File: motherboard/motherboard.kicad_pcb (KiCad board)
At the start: 4 copper layers, 132.9 x 92 mm, 265 parts, among them CN1 PJ-332A-6A (3.5mm Jack), IC1 PI6C557-05BLE, J1 USB_C_Receptacle, J10 DEBUG UART, J11 SYSTEM, J12 5V FAN, J13 Bus_M.2_Socket_E, J14 Micro_SD_Card_Det1, J15 Bus_M.2_Socket_M, J16 USB, J17 USB, J18 USB, J19 USB, J2 20455-040E-76 OLED IPEX, J20 CM3588 Hirose Connector, J22 BATTERY IN, J3 RIGHT SPEAKERS, J4 LEFT SPEAKERS, J5 Outer USB-C, J6 OLED EL POWER, J7 HALL SWITCH, J8 HDMI_A, Q1 2SK3018W, Q10 2SK3018W, Q11 AO3415A, Q12 2SK3018W, Q2 2SK3018W, Q3 L2N7002WT1G, Q4 2SK3018W, Q5 2SK3018W, Q6 WNM6002-3/TR, Q7 WNM6002-3/TR, Q8 WNM6002-3/TR, Q9 WNM6002-3/TR, SW1 PWR, SW2 RESET, SW3 MASK, SW4 RECOVERY, U1 TPD4E02B04, U10 TPD4E02B04, U11 TPD4E02B04, U12 TPD4E02B04, U13 TPD4E02B04, U14 AP2331, U15 TVS2200DRV, U16 TPA2016D2RTJR, U17 TPS564257DRLR, U18 TPD4E02B04, U19 TPD4E02B04, U2 TPD4E02B04, U20 TPS564257DRLR, U21 AP2127K-3.3, U22 CH334F, U23 TPS564257DRLR, U26 AMS1117-1.8, U28 SPI Flash, U29 TVS2200DRV, U3 TPD4E02B04, U4 FUSB302BMPX, U5 SY6280AAC, U6 SY6280AAC, U7 FUSB302BMPX, U8 TPD4E02B04, U9 TPD4E02B04, Y1 25MHz, Y2 12MHz

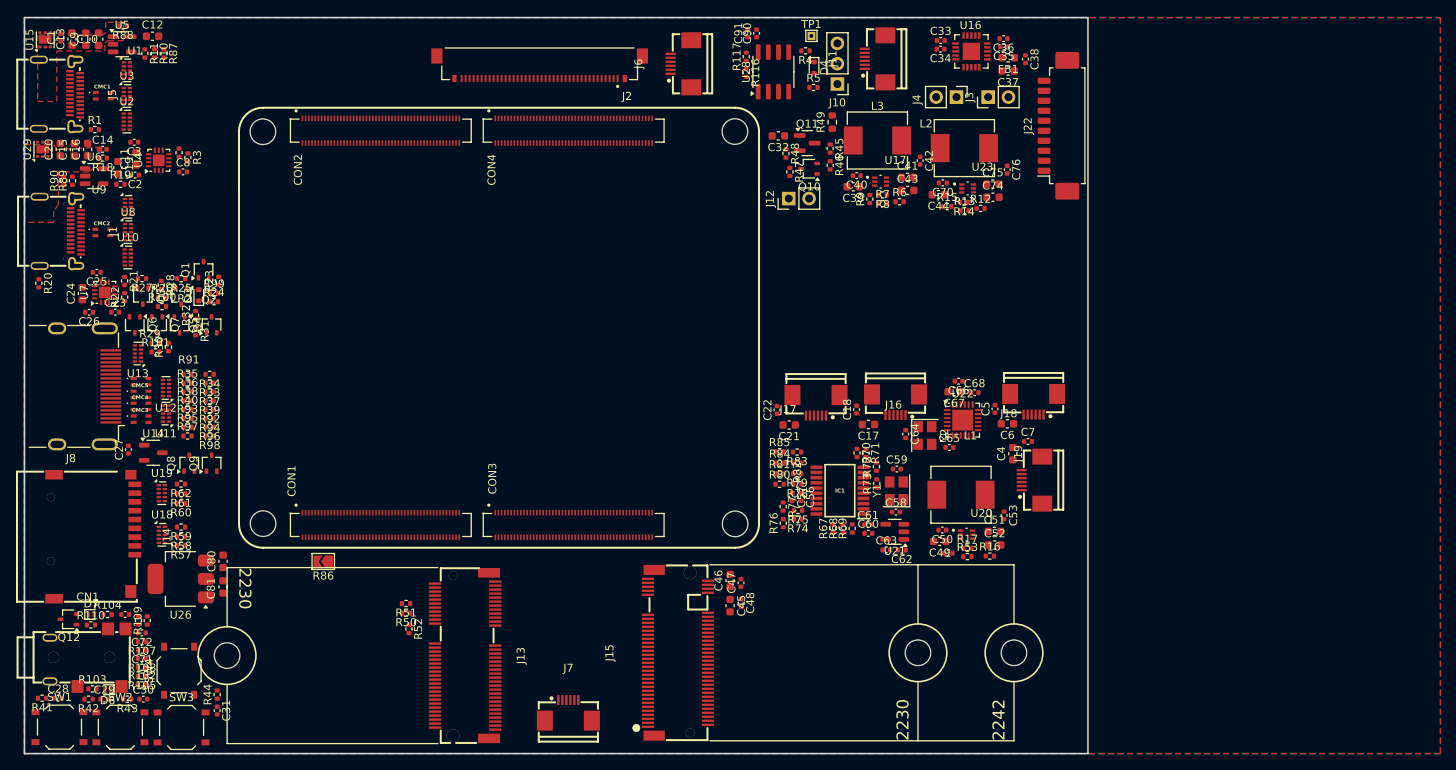
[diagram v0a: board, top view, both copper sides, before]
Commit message: 6 layer for better high speed signaling integrity
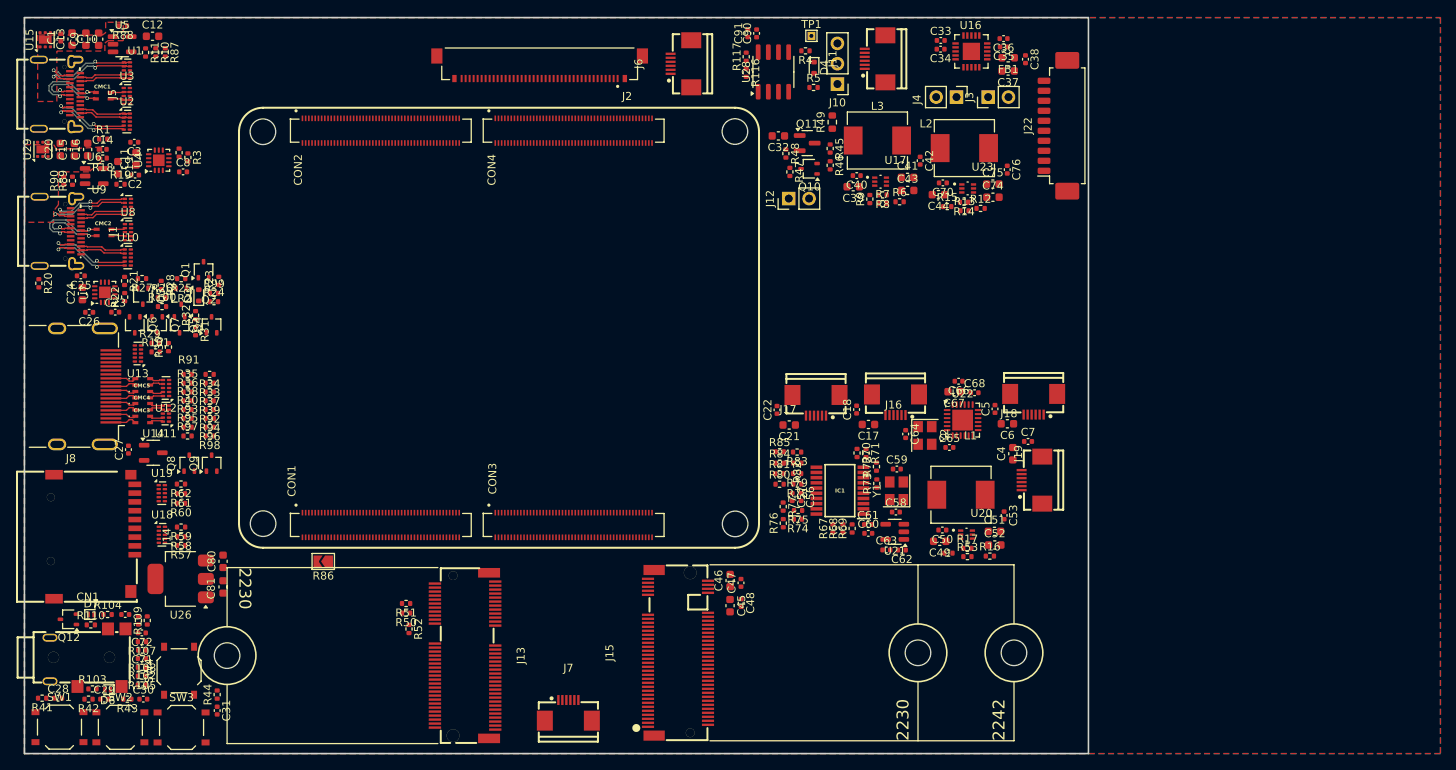
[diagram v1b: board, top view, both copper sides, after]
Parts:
- R54: renamed from 10k; value Resistor_SMD:R_0402_1005Metric -> 10k
- moved C25 2.04 mm to (63.4, 83.7)
- moved R1 1.58 mm to (66.2, 66.6)
- moved CMC3 0.21 mm to (71.1, 101.7)
- moved CMC4 0.21 mm to (71.1, 100.0)
- moved CMC5 0.21 mm to (71.1, 98.5)
- moved CMC6 0.21 mm to (71.1, 97.0)
- moved R10 0.21 mm to (72.8, 55.8)
- moved R87 0.21 mm to (74.0, 55.8)
- moved CMC2 0.16 mm to (66.3, 78.3)
- moved R11 0.15 mm to (71.5, 55.8)
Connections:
- net Net-(CMC2-Pad1) renamed /USBC1/IN_D+
- net Net-(CMC2-Pad2) renamed /USBC1/IN_D-
- CMC3 pad 1: unconnected-(CMC3-Pad1) -> /HDMI_TX/IN_TX2N
- CMC3 pad 2: unconnected-(CMC3-Pad2) -> /HDMI_TX/IN_TX2P
- CMC4 pad 1: unconnected-(CMC4-Pad1) -> /HDMI_TX/IN_TX1N
- CMC4 pad 2: unconnected-(CMC4-Pad2) -> /HDMI_TX/IN_TX1P
- CMC5 pad 1: unconnected-(CMC5-Pad1) -> /HDMI_TX/IN_TX0N
- CMC5 pad 2: unconnected-(CMC5-Pad2) -> /HDMI_TX/IN_TX0P
- CMC6 pad 1: unconnected-(CMC6-Pad1) -> /HDMI_TX/IN_TX3N
- CMC6 pad 2: unconnected-(CMC6-Pad2) -> /HDMI_TX/IN_TX3P
- J8 pad 1: unconnected-(CMC3-Pad2) -> /HDMI_TX/IN_TX2P
- J8 pad 10: unconnected-(CMC6-Pad2) -> /HDMI_TX/IN_TX3P
- J8 pad 12: unconnected-(CMC6-Pad1) -> /HDMI_TX/IN_TX3N
- J8 pad 3: unconnected-(CMC3-Pad1) -> /HDMI_TX/IN_TX2N
- J8 pad 4: unconnected-(CMC4-Pad2) -> /HDMI_TX/IN_TX1P
- J8 pad 6: unconnected-(CMC4-Pad1) -> /HDMI_TX/IN_TX1N
- J8 pad 7: unconnected-(CMC5-Pad2) -> /HDMI_TX/IN_TX0P
- J8 pad 9: unconnected-(CMC5-Pad1) -> /HDMI_TX/IN_TX0N
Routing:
- net /USBC0/RX1+: track 0.00 -> 13.1 mm, vias 0 -> 2
- net /USBC0/RX1-: track 0.00 -> 12.9 mm, vias 0 -> 2
- net /USBC0/IN_D+: track 0.00 -> 11.7 mm, vias 0 -> 2
- net /USBC1/RX1-: track 0.00 -> 11.5 mm, vias 0 -> 2
- net /USBC1/IN_D+: track 0.00 -> 11.4 mm, vias 0 -> 2
- net /USBC1/TX2-: track 0.00 -> 11.2 mm, vias 0 -> 2
- net /USBC1/TX2+: track 0.00 -> 11.1 mm, vias 0 -> 2
- net /USBC1/RX1+: track 0.00 -> 10.7 mm, vias 0 -> 2
- net /USBC0/TX2-: track 0.00 -> 10.3 mm, vias 0 -> 2
- net /USBC0/IN_D-: track 0.00 -> 10.3 mm, vias 0 -> 2
- net /USBC0/TX2+: track 0.00 -> 10.3 mm, vias 0 -> 2
- net /USBC1/IN_D-: track 0.00 -> 10.2 mm, vias 0 -> 2
- net /USBC0/RX2-: track 0.00 -> 6.54 mm
- net /USBC0/RX2+: track 0.00 -> 6.54 mm
- net /USBC0/TX1+: track 0.00 -> 6.48 mm
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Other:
- board size 132.9 x 92 mm -> 133 x 92 mm
- copper layers 4 -> 6

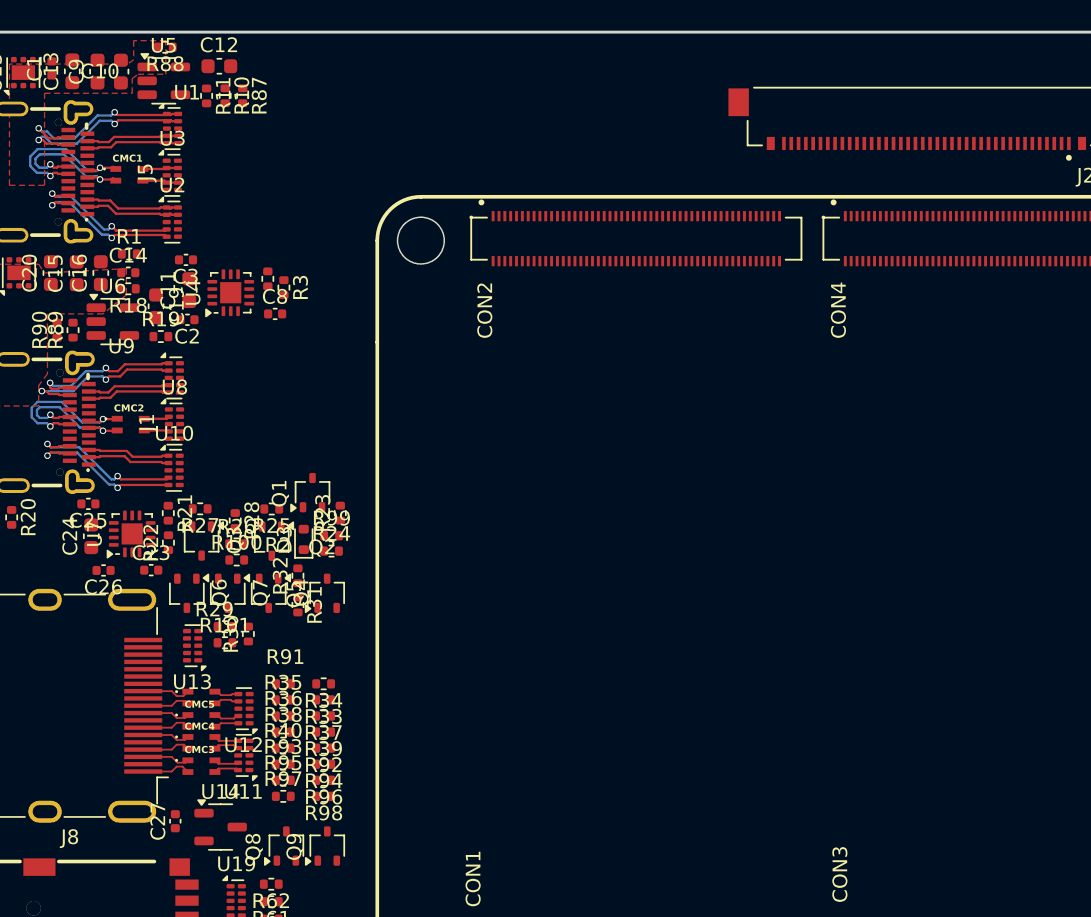
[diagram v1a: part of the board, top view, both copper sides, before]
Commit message: rerouting high speed traces
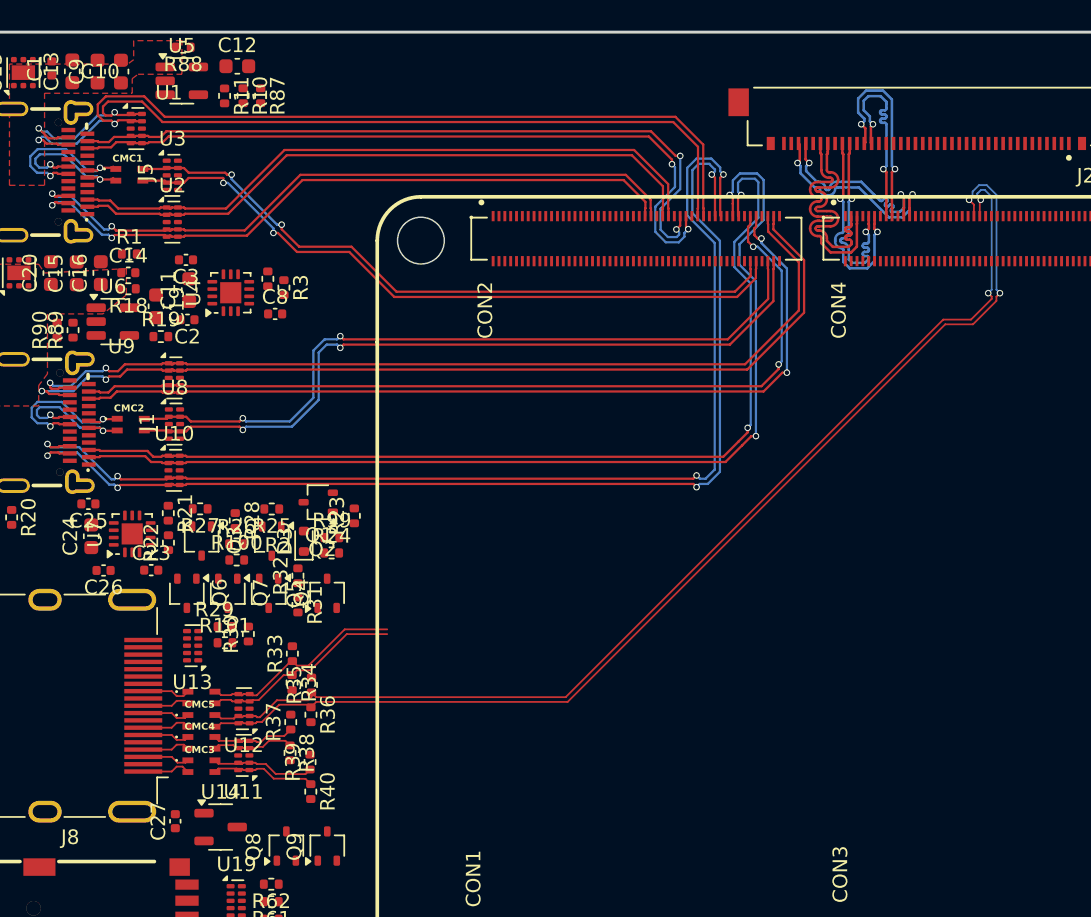
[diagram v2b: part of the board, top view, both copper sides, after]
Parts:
- removed R91, R92, R94, R96, R98: 510, Resistor_SMD:R_0402_1005Metric
- removed R93, R95, R97: 24k, Resistor_SMD:R_0402_1005Metric
- Q2: value 2SK3018W -> Q2
- R33, R34, R36, R38, R40: value 24k -> 499R
- R35, R37, R39: value 510 -> 499R
- U1: value TPD4E02B04 -> U1
- moved R33 3.82 mm to (77.4, 94.0), turned to 90 degrees
- moved R40 3.52 mm to (78.6, 103.4), turned to -90 degrees
- moved U1 2.48 mm to (66.7, 58.0)
- moved R37 2.29 mm to (77.2, 98.6), turned to 90 degrees
- moved R39 2.26 mm to (78.6, 101.4), turned to 90 degrees
- moved R35 2.19 mm to (78.7, 96.1), turned to 90 degrees
- moved R34 2.16 mm to (77.3, 95.9), turned to -90 degrees
- moved R36 1.89 mm to (78.6, 98.1), turned to -90 degrees
- moved R38 1.50 mm to (77.2, 100.7), turned to -90 degrees
- moved C12 1.23 mm to (73.6, 53.8)
- moved R11 1.23 mm to (72.7, 55.8)
- moved R87 1.23 mm to (75.2, 55.8)
- moved R88 1.23 mm to (69.9, 52.5)
- moved U5 1.23 mm to (69.8, 54.8)
- moved R10 1.23 mm to (74.0, 55.8)
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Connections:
- R33 pad 1: /HDMI_TX/HDMI0_TX3P -> /HDMI_TX/HDMI0_TX3N
- R34 pad 1: /HDMI_TX/HDMI0_TX3N -> /HDMI_TX/HDMI0_TX3P
- R35 pad 1: /HDMI_TX/HDMI0_TX3P -> /HDMI_TX/HDMI0_TX0N
- R35 pad 2: Net-(Q6-D) -> Net-(Q7-D)
- R36 pad 1: /HDMI_TX/HDMI0_TX0N -> /HDMI_TX/HDMI0_TX0P
- R37 pad 1: /HDMI_TX/HDMI0_TX0N -> /HDMI_TX/HDMI0_TX1N
- R37 pad 2: Net-(Q7-D) -> Net-(Q8-D)
- R38 pad 1: /HDMI_TX/HDMI0_TX0P -> /HDMI_TX/HDMI0_TX1P
- R38 pad 2: Net-(Q7-D) -> Net-(Q8-D)
- R39 pad 1: /HDMI_TX/HDMI0_TX0P -> /HDMI_TX/HDMI0_TX2N
- R39 pad 2: Net-(Q7-D) -> Net-(Q9-D)
- R40 pad 1: /HDMI_TX/HDMI0_TX1N -> /HDMI_TX/HDMI0_TX2P
- R40 pad 2: Net-(Q8-D) -> Net-(Q9-D)
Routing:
- net /HDMI_TX/HDMI0_TX0P: track 1.70 -> 77.2 mm, vias 0 -> 2
- net /HDMI_TX/HDMI0_TX0N: track 1.78 -> 75.9 mm, vias 0 -> 2
- net /USBC1/TX2-: track 11.2 -> 76.8 mm, vias 2 -> 4
- net /USBC1/TX2+: track 11.1 -> 76.1 mm, vias 2 -> 4
- net /USBC1/RX2+: track 5.67 -> 70.5 mm, vias 0 -> 2
- net /USBC1/RX2-: track 5.67 -> 68.5 mm, vias 0 -> 2
- net /USBC1/TX1-: track 5.70 -> 60.5 mm, vias 0 -> 2
- net /USBC1/TX1+: track 5.70 -> 59.8 mm, vias 0 -> 2
- net /USBC1/RX1-: track 11.5 -> 64.2 mm
- net /USBC1/RX1+: track 10.7 -> 62.8 mm
- net /USBC1/D-: track 1.71 -> 51.8 mm, vias 0 -> 2
- net /USBC1/D+: track 1.74 -> 51.2 mm, vias 0 -> 2
- net /USBC0/RX1-: track 12.9 -> 60.5 mm
- net /USBC0/RX1+: track 13.1 -> 58.9 mm
- net /USBC0/D-: track 2.46 -> 47.6 mm, vias 0 -> 2
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
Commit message: v0.2 progress
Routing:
- net /SDMMC0_D2: track 0.00 -> 116.8 mm
- net /SDMMC0_D3: track 0.00 -> 115.4 mm
- net /SDMMC0_CMD: track 0.00 -> 113.7 mm
- net /SDMMC0_D0: track 0.00 -> 110.0 mm
- net /HDMI_TX/HDMI0_TX2N: track 7.16 -> 116.7 mm, vias 0 -> 2
- net /HDMI_TX/HDMI0_TX2P: track 7.25 -> 116.1 mm, vias 0 -> 2
- net /SDMMC0_D1: track 0.00 -> 108.1 mm
- net /GPIO0_A4/SDMMC_DET_L: track 0.00 -> 106.1 mm
- net /HDMI_TX/HDMI0_TX1P: track 5.73 -> 108.1 mm, vias 0 -> 2
- net /HDMI_TX/HDMI0_TX1N: track 5.77 -> 106.5 mm, vias 0 -> 2
- net /HDMI_TX/HDMI0_TX3P: track 13.9 -> 89.7 mm, vias 0 -> 2
- net /HDMI_TX/HDMI0_TX3N: track 14.2 -> 88.3 mm, vias 0 -> 2
- net /USBC0/VBUS: track 0.00 -> 26.9 mm, vias 0 -> 2
- net /USBC0/CC2: track 0.00 -> 26.1 mm, vias 0 -> 2
- net unconnected-(R1-Pad1): track 0.00 -> 21.5 mm
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
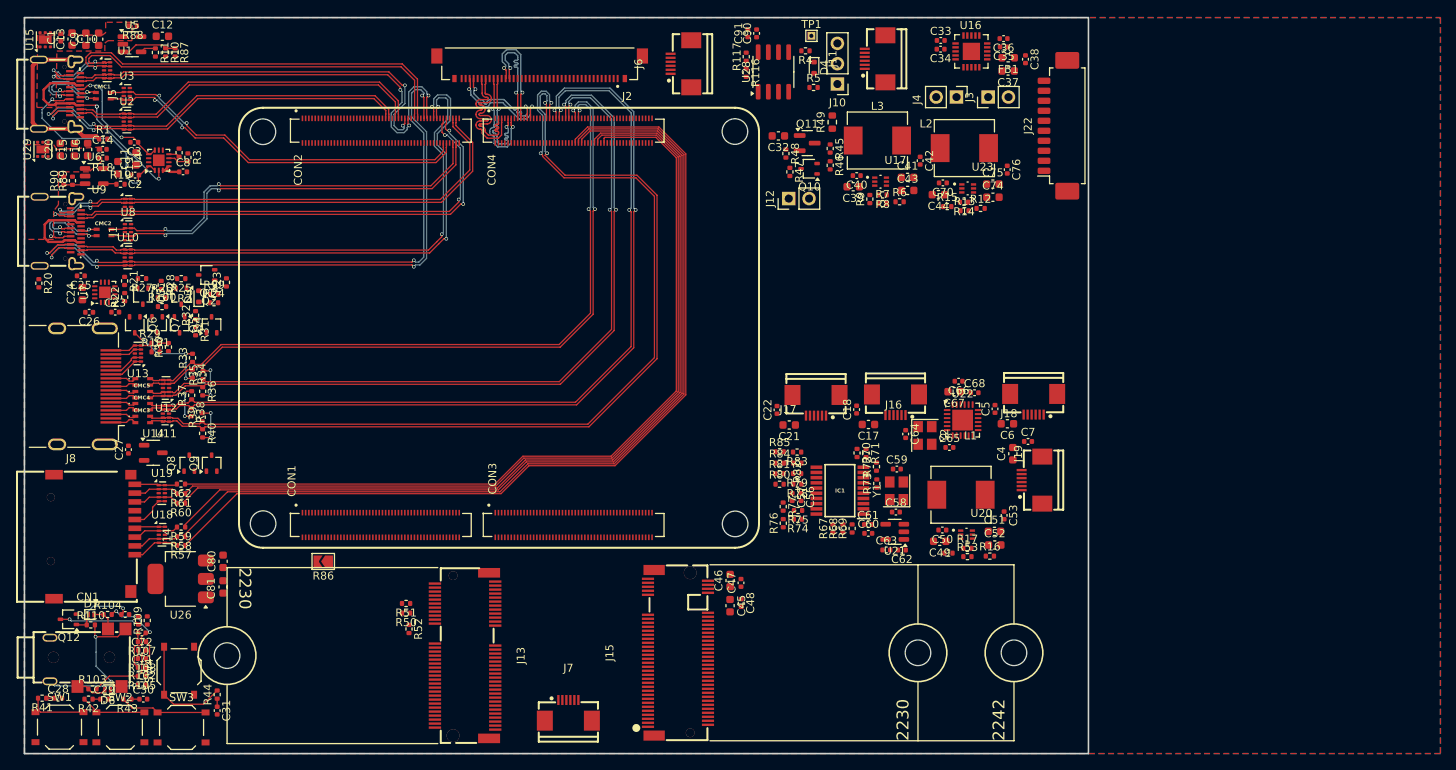
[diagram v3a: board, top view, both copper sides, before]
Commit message: v0.2 good routing checkpoint (217 unrouted)
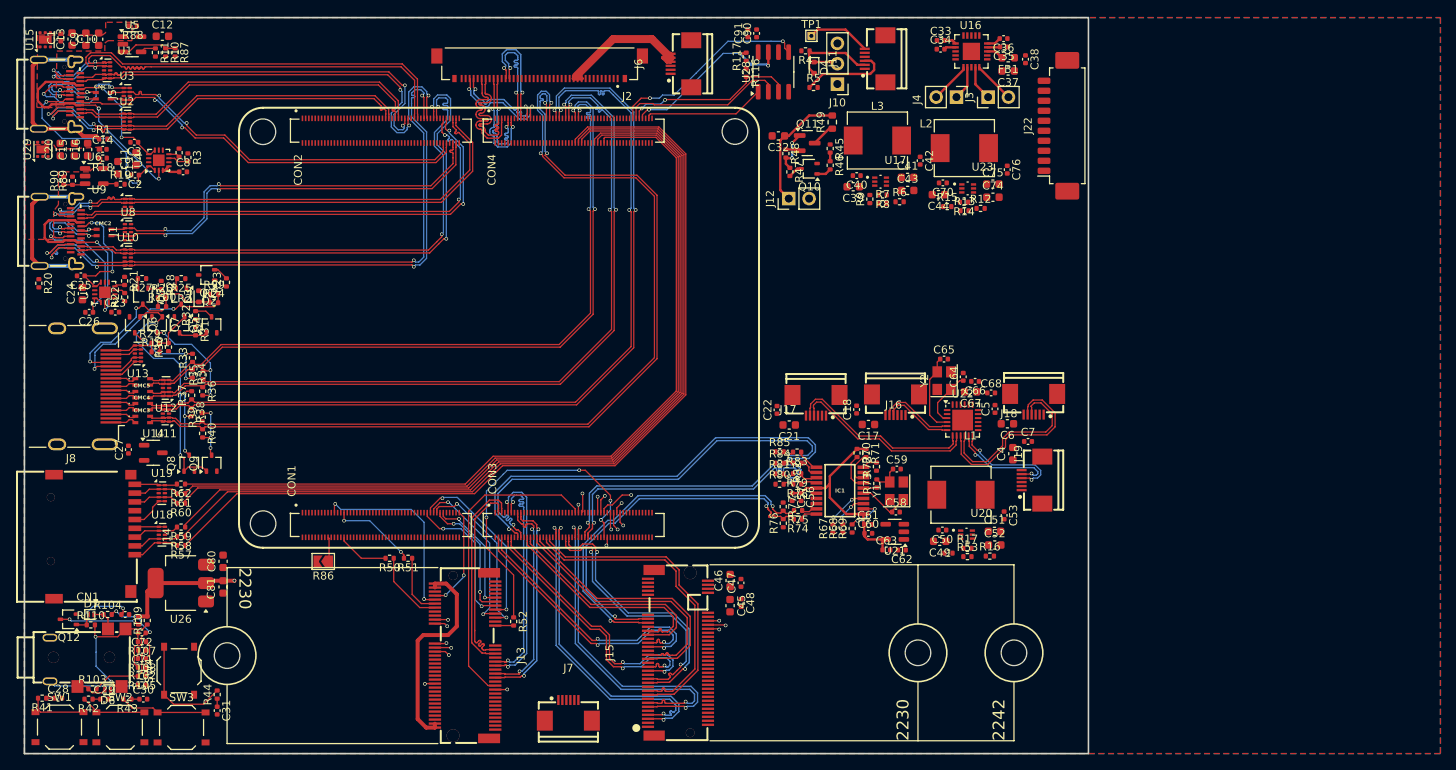
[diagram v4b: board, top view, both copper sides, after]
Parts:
- Q2: value Q2 -> 2SK3018W
- U1: value U1 -> TPD4E02B04
- moved R52 13.1 mm to (117.5, 126.9)
- moved C65 11.1 mm to (171.3, 94.1)
- moved C64 10.1 mm to (173.7, 96.3), turned to 90 degrees
- moved Y2 7.25 mm to (171.3, 96.8), turned to 90 degrees
- moved R50 7.15 mm to (102.0, 119.0)
- moved R51 5.66 mm to (104.3, 119.0)
- moved C66 2.07 mm to (175.2, 96.9)
- moved C67 2.07 mm to (174.6, 98.2)
- moved C68 2.07 mm to (177.2, 98.3)
- moved U26 0.52 mm to (75.9, 122.1)
- turned C34 to 0 degrees
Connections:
- net /USB2.0/DM1 renamed /USB2.0/D1_N
- net /USB2.0/DM2 renamed /USB2.0/D2_N
- net /USB2.0/DM3 renamed /USB2.0/D3_N
- net /USB2.0/DM4 renamed /USB2.0/D4_N
- net /USB2.0/DP1 renamed /USB2.0/D1_P
- net /USB2.0/DP2 renamed /USB2.0/D2_P
- net /USB2.0/DP3 renamed /USB2.0/D3_P
- net /USB2.0/DP4 renamed /USB2.0/D4_P
- net /USB20_HOST0_DM renamed /USB20_HOST0_DN
- net /USB20_HOST1_DM renamed /USB20_HOST1_DN
- C34 pad 1: Net-(C34-Pad1) -> GND
- C35 pad 1: Net-(C34-Pad1) -> GND
- U16 pad 17: /Audio/AMP_SDA -> /I2C6_SDA_M0
- U16 pad 19: /Audio/AMP_SCL -> /I2C6_SCL_M0
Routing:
- net /PCIE30_PORT0_REFCLKP: track 0.00 -> 56.6 mm, vias 0 -> 2
- net /PCIE30_PORT0_REFCLKN: track 0.00 -> 56.4 mm, vias 0 -> 2
- net /GPIO4_A2: track 0.00 -> 49.8 mm, vias 0 -> 2
- net /PCIE3.0-MKEY/PCIE30_REFCLK_A_N: track 0.00 -> 46.3 mm, vias 0 -> 2
- net /PCIE3.0-MKEY/PCIE30_REFCLK_A_P: track 0.00 -> 46.3 mm, vias 0 -> 2
- net /PCIE30_PORT1_TX3N: track 0.00 -> 41.1 mm, vias 0 -> 2
- net /PCIE30_PORT1_TX3P: track 0.00 -> 41.0 mm, vias 0 -> 2
- net /GPIO0_C4/UART0_RX_M0: track 0.00 -> 41.0 mm, vias 0 -> 4
- net /GPIO4_A1/TP_2_RST_L: track 0.00 -> 39.6 mm, vias 0 -> 2
- net /PCIE30_PORT1_RX3N: track 0.00 -> 39.3 mm, vias 0 -> 2
- net /PCIE30_PORT1_RX3P: track 0.00 -> 39.2 mm, vias 0 -> 2
- net /PCIE30_PORT1_RX2N: track 0.00 -> 39.2 mm
- net /PCIE30_PORT1_RX2P: track 0.00 -> 39.2 mm
- net /GPIO4_A0/TP_2_INT_L: track 0.00 -> 39.0 mm
- net /PCIE30_PORT1_REFCLKN: track 0.00 -> 38.1 mm, vias 0 -> 2
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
